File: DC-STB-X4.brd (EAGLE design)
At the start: 29 x 54 mm, 2 parts

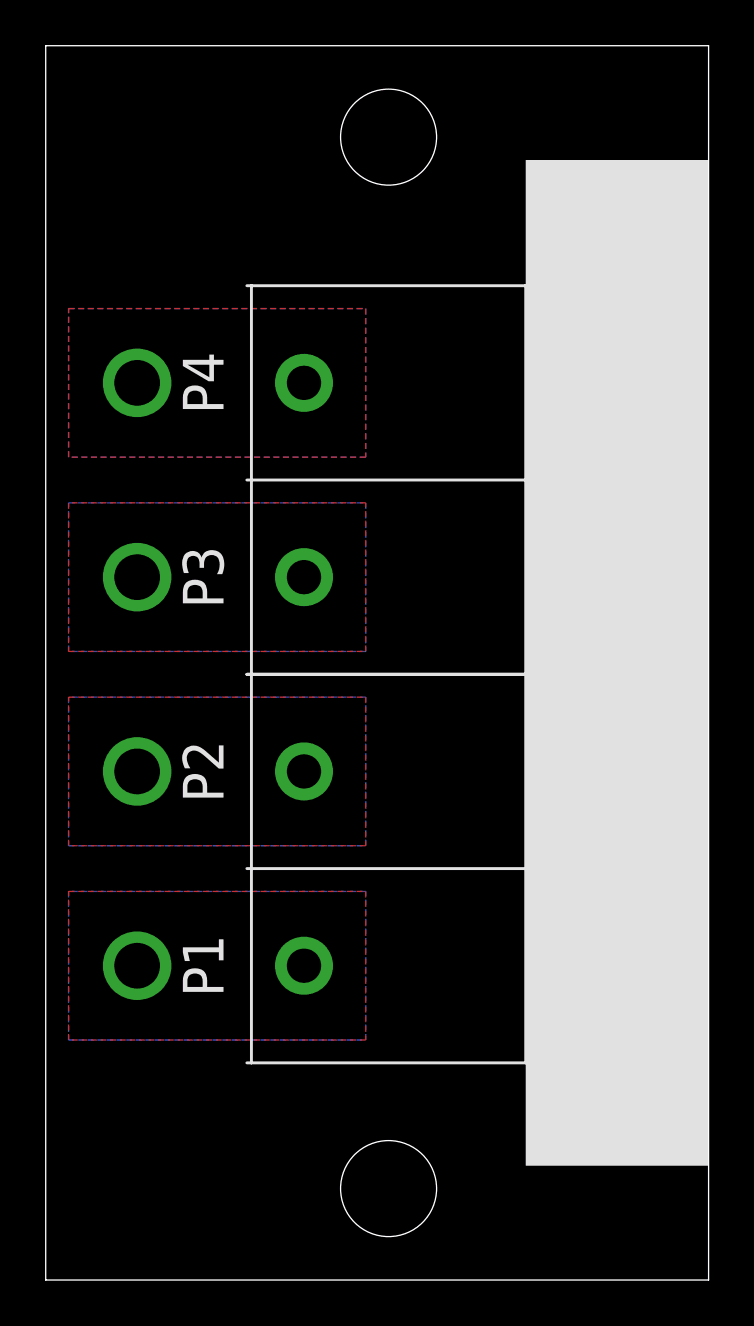
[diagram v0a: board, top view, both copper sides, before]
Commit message: made x4 board smaller. Generated CAM files. Generated PNG preview.
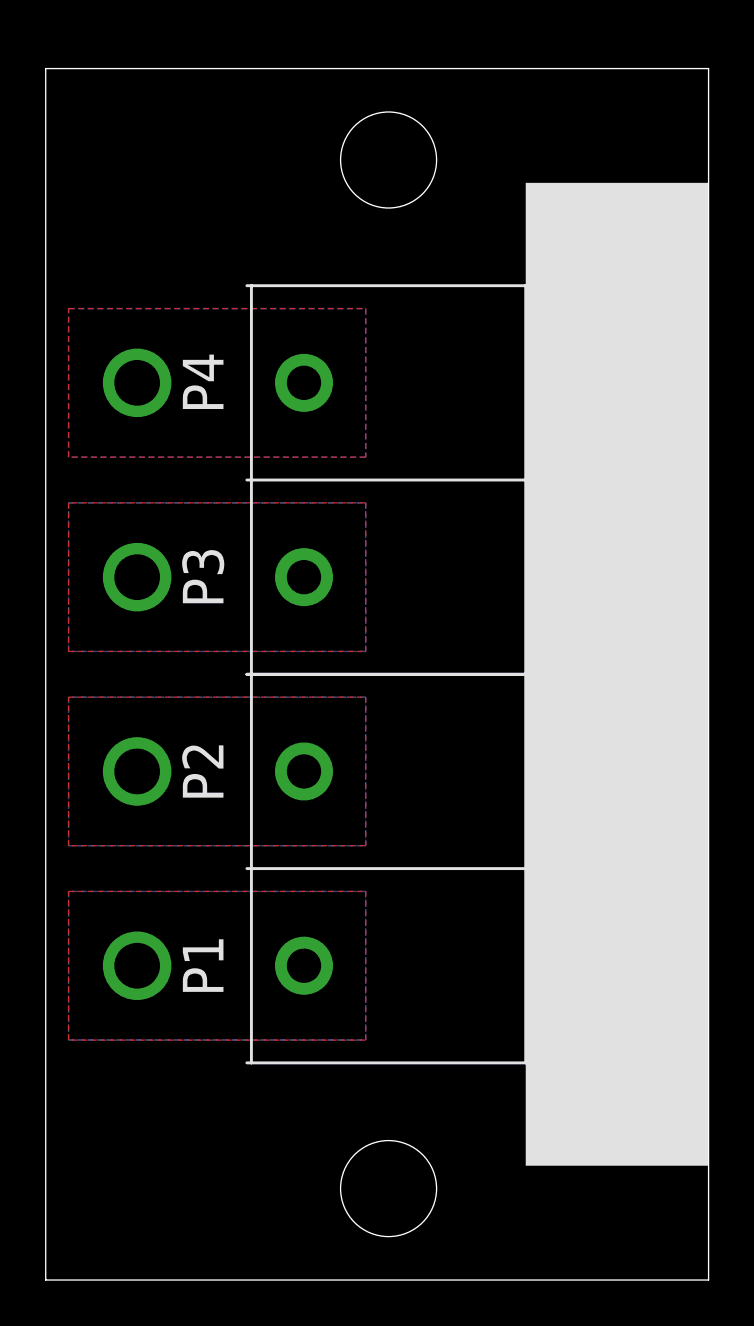
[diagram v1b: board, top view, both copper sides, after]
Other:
- board size 29 x 54 mm -> 29 x 53 mm
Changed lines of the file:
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@@
 <drawing>
 <settings>
-<setting alwaysvectorfont="yes"/>
+<setting alwaysvectorfont="no"/>
 <setting verticaltext="up"/>
 </settings>
@@
 <plain>
 <wire x1="0" y1="0" x2="29" y2="0" width="0" layer="20"/>
-<wire x1="29" y1="0" x2="29" y2="54" width="0" layer="20"/>
-<wire x1="29" y1="54" x2="0" y2="54" width="0" layer="20"/>
-<wire x1="0" y1="54" x2="0" y2="0" width="0" layer="20"/>
+<wire x1="29" y1="0" x2="29" y2="53" width="0" layer="20"/>
+<wire x1="29" y1="53" x2="0" y2="53" width="0" layer="20"/>
+<wire x1="0" y1="53" x2="0" y2="0" width="0" layer="20"/>
 <hole x="15" y="4" drill="4.2"/>
-<hole x="15" y="50" drill="4.2"/>
+<hole x="15" y="49" drill="4.2"/>
 <circle x="15" y="4" radius="4.5" width="0.127" layer="51"/>
-<circle x="15" y="50" radius="4.5" width="0.127" layer="51"/>
+<circle x="15" y="49" radius="4.5" width="0.127" layer="51"/>
 <text x="28" y="38" size="1.778" layer="22" font="vector" rot="MR270">DC-STB-X4-0010
 (c) Andriy Golovnya
 http://redscorp.net</text>
-<rectangle x1="21" y1="5" x2="29" y2="49" layer="21"/>
+<rectangle x1="21" y1="5" x2="29" y2="48" layer="21"/>
 <text x="6" y="13.75" size="1.778" layer="21" font="vector" rot="R90" align="top-center">P1</text>
 <text x="6" y="22.25" size="1.778" layer="21" font="vector" rot="R90" align="top-center">P2</text>

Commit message: Added logos to all boards. Generated CAM files.
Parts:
- added LOGO1: MFDECLOGO_L_10MM, _my_logos:MFDEC_L_10MM
- added LOGO2: RSNURL_QR_10MM, _my_logos:RSNURL_QR_10MM
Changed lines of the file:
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@@
 <layer number="97" name="Info" color="7" fill="1" visible="no" active="no"/>
 <layer number="98" name="Guide" color="6" fill="1" visible="no" active="no"/>
+<layer number="200" name="200bmp" color="1" fill="10" visible="yes" active="yes"/>
 </layers>
 <board>
@@
 <element name="U$1" library="KF8500-Terminals" package="KF8500-8.5-2P" value="KF8500-8.5-2P" x="15" y="18" smashed="yes" rot="R90"/>
 <element name="U$2" library="KF8500-Terminals" package="KF8500-8.5-2P" value="KF8500-8.5-2P" x="15" y="35" smashed="yes" rot="R90"/>
+<element name="LOGO1" library="_my_logos" package="MFDEC_L_10MM" value="MFDECLOGO_L_10MM" x="15" y="41" smashed="yes" rot="MR0"/>
+<element name="LOGO2" library="_my_logos" package="RSNURL_QR_10MM" value="RSNURL_QR_10MM" x="11" y="1" smashed="yes" rot="MR0"/>
 </elements>
 <signals>
